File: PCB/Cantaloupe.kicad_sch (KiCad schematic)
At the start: 117 parts, among them J1 RGB_Out, J2 SWD, J3 Trackpad, J4 OLED, J5 Extra, J6 USB_In, J7 Split_comm_link, Q1 AO6802, SW1 MX, SW10 MX, SW11 MX, SW12 MX, SW13 MX, SW14 MX, SW15 MX, SW16 MX, SW17 MX, SW18 MX, SW19 MX, SW2 MX, SW20 MX, SW21 MX, SW22 MX, SW23 MX, SW24 MX, SW25 MX, SW26 MX, SW27 MX, SW28 MX, SW29 MX, SW3 MX, SW30 MX, SW31 Encoder, SW32 Reset, SW4 MX, SW5 MX, SW6 MX, SW7 MX, SW8 MX, SW9 MX, U1 STM32F401CCU6, U2 MB85RS64, U3 SRV05-4, U4 SRV05-4, U5 W25Q128JVS, U6 XC6206P332MR, Y1 8MHz

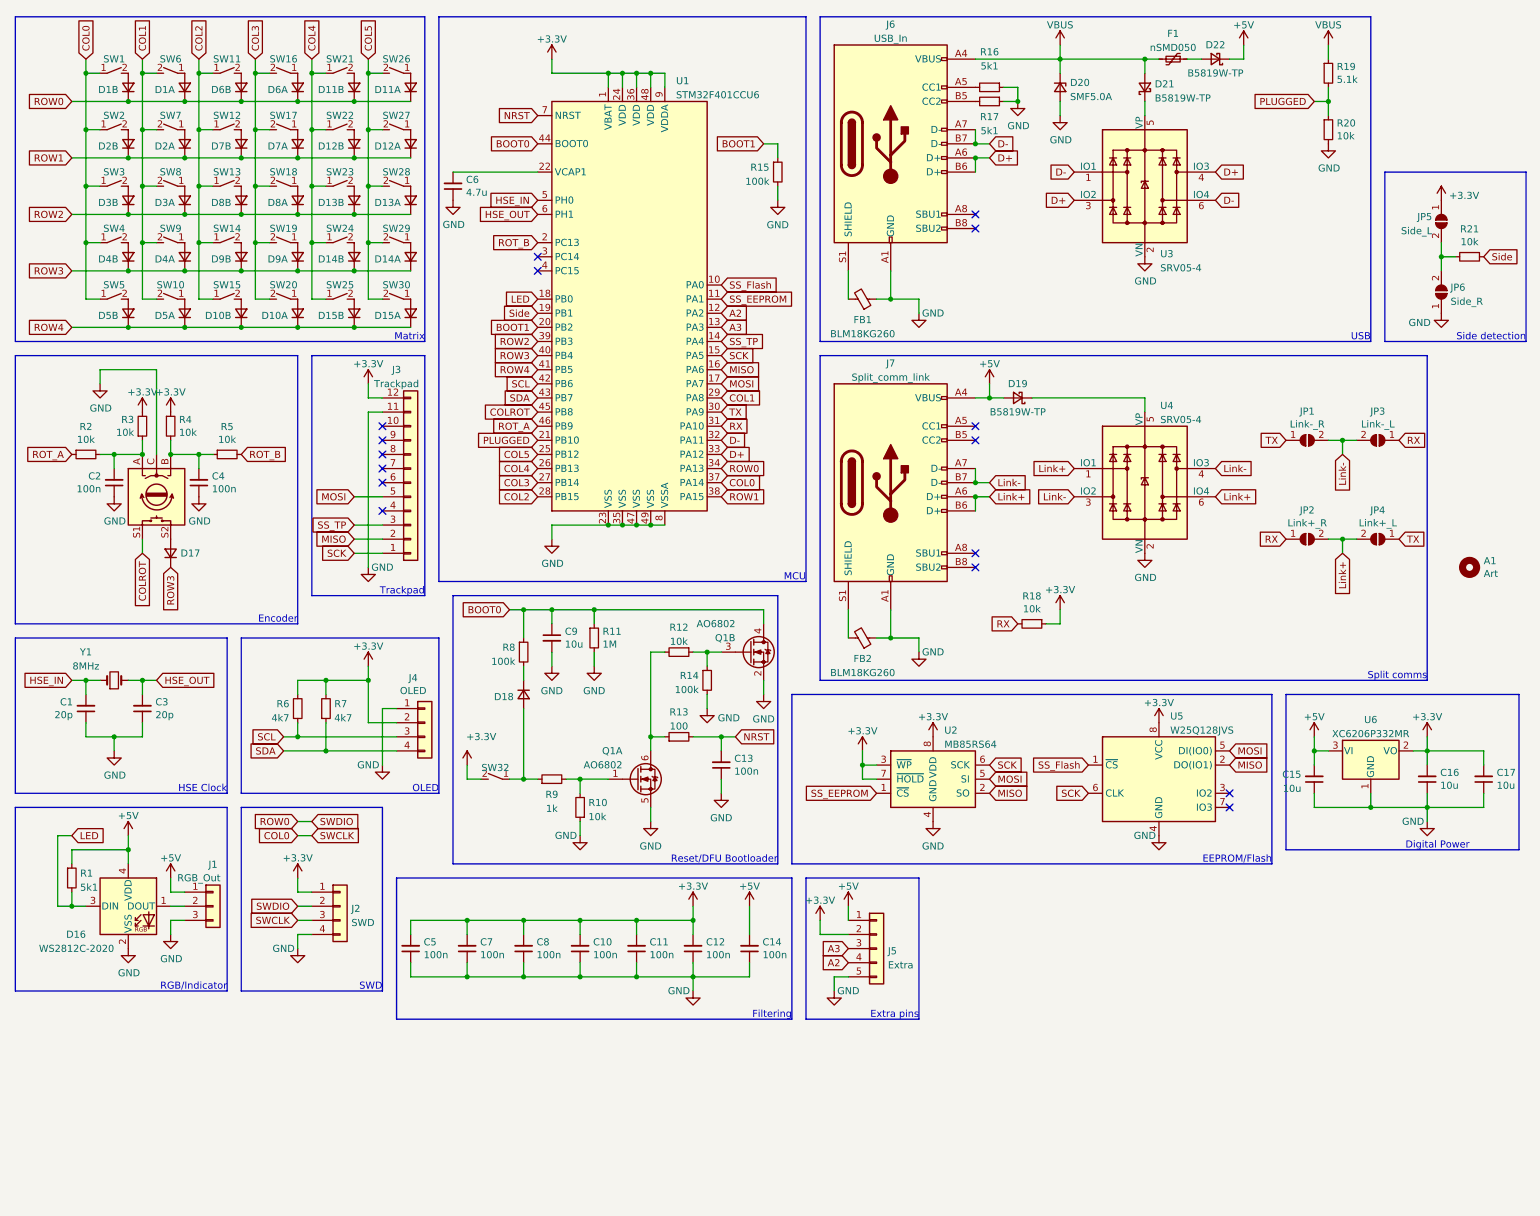
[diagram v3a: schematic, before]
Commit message: 30/5/2022 changes
Changed XC6206P332MR-G to XC6220B331MR-G for more power output. Changed fuse to 1A. Fixed library links. Changed AO6802 back to two AO3400s. Moved reset circuit downwards and extra pin header upwards for better routing. Updated BOM.
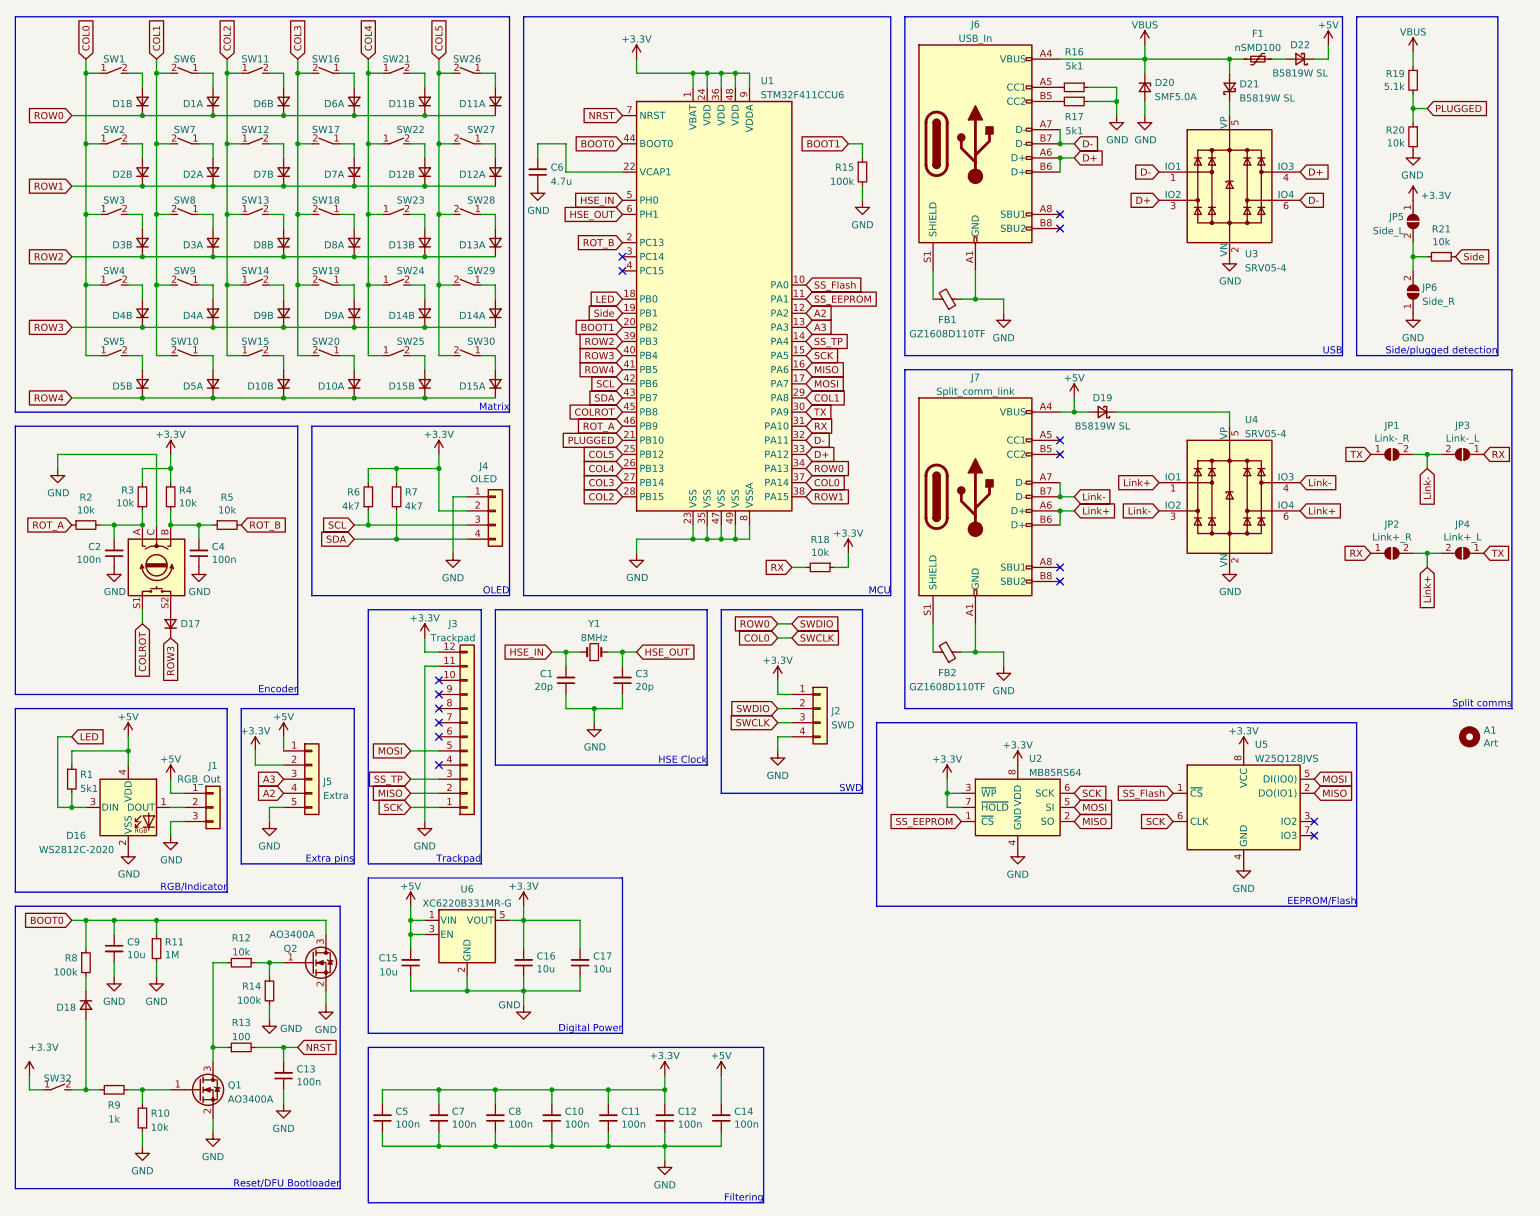
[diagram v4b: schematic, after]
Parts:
- removed Q1: AO6802, Package_TO_SOT_SMD:SOT-23-6, symbol Device:Q_Dual_NMOS_G1S2G2D2S1D1
- removed U6: XC6206P332MR, Package_TO_SOT_SMD:SOT-23, symbol Regulator_Linear:XC6206PxxxMR
- added Q1, Q2: AO3400A, Package_TO_SOT_SMD:SOT-23, symbol Transistor_FET:AO3400A
- added U6: XC6220B331MR-G, Package_TO_SOT_SMD:SOT-23-5, symbol Regulator_Linear:AP2112K-3.3
- A1: footprint Ariamelon:Ariamelon_Logo_x3_CU -> Cantaloupe:Ariamelon_Logo_x3_CU
- D1, D10, D11, D12, D13, D14, D15, D2, D3, D4, D5, D6, D7, D8, D9: symbol Ariamelon:D_Dual_CommonCathode_AAK_Split_Small -> Cantaloupe:D_Dual_CommonCathode_AAK_Split_Small
- D16: footprint Ariamelon:LED_WS2812-2020_Flippable -> Cantaloupe:LED_WS2812-2020_Flippable; LCSC part number C965556 -> C2976072
- D17, D18, D20: footprint Ariamelon:D_SOD-123 -> Cantaloupe:D_SOD-123
- D19, D21, D22: value B5819W-TP -> B5819W SL; footprint Ariamelon:D_SOD-123 -> Cantaloupe:D_SOD-123
- F1: value nSMD050 -> nSMD100; LCSC part number C69688 -> C66453
- FB1, FB2: value BLM18KG260 -> GZ1608D110TF; LCSC part number C88981 -> C74329
- J1: footprint Ariamelon:PinHeader_1x03_P2.54mm_Vertical_Silkless -> Cantaloupe:PinHeader_1x03_P2.54mm_Vertical_Silkless
- J2: footprint Ariamelon:PinHeader_1x04_P2.54mm_Vertical_SIlkless -> Cantaloupe:PinHeader_1x04_P2.54mm_Vertical_SIlkless
- J3: footprint Ariamelon:Hirose_FH12-12S-0.5SH_1x12-1MP_P0.50mm_Horizontal_Flippable -> Cantaloupe:Hirose_FH12-12S-0.5SH_1x12-1MP_P0.50mm_Horizontal_Flippable
- J4: footprint Ariamelon:OLED_0.96_SSD1306_128x64_Flippable_Reversepads -> Cantaloupe:OLED_0.96_SSD1306_128x64_Flippable_Reversepads
- J5: footprint Ariamelon:PinHeader_1x05_P2.54mm_Vertical_Silkless -> Cantaloupe:PinHeader_1x05_P2.54mm_Vertical_Silkless
- J6, J7: footprint Ariamelon:HRO-TYPE-C-31-M-13x -> Cantaloupe:HRO-TYPE-C-31-M-13x; symbol Ariamelon:USB_C_Receptacle_USB2.0-Connector -> Cantaloupe:USB_C_Receptacle_USB2.0-Connector
- SW1, SW10, SW11, SW12, SW13, SW14, SW15, SW16, SW17, SW18, SW19, SW2, SW20, SW21, SW22, SW23, SW24, SW25, SW26, SW27, SW28, SW29, SW3, SW30, SW4, SW5, SW6, SW7, SW8, SW9: footprint Ariamelon:MXOnly-1U-Hotswap-Dual -> Cantaloupe:MXOnly-1U-Hotswap-Dual; symbol Ariamelon:SW_SPST_Small -> Cantaloupe:SW_SPST_Small
- SW31: footprint Ariamelon:EC11_Flippable -> Cantaloupe:EC11_Flippable
- SW32: footprint Ariamelon:Switch_TS24ZJ_Flippable -> Cantaloupe:Switch_TS24ZJ_Flippable; symbol Ariamelon:SW_SPST_Small -> Cantaloupe:SW_SPST_Small
- U1: value STM32F401CCU6 -> STM32F411CCU6
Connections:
- net +3V3: now also SW32.1 (A), U6.5 (VOUT); no longer SW32.2 (B)
- net +5V: now also U6.1 (VIN), U6.3 (EN)
- net BOOT0: now also Q2.3 (D)
- net GND: now also Q1.2 (S), Q2.2 (S), U6.2 (GND)
- net at D18.2 (A), R9.1: now also SW32.2 (B); no longer SW32.1 (A)
- net at R10.2, R9.2: now also Q1.1 (G)
- net at R12.2, R13.1: now also Q1.3 (D)
- net at R12.1, R14.1: now also Q2.1 (G)
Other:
- note added: "Side/plugged detection"
- note removed: "Side detection"
- title: (none) -> Cantaloupe split ergonomic keyboard
- moved on the sheet: A1, C1, C10, C11, C12, C13, C14, C15, C17, C2, C3, C4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

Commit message: Better routing
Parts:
- SW1, SW10, SW11, SW12, SW13, SW14, SW15, SW16, SW17, SW18, SW19, SW2, SW20, SW21, SW22, SW23, SW24, SW25, SW26, SW27, SW28, SW29, SW3, SW30, SW4, SW5, SW6, SW7, SW8, SW9: footprint Cantaloupe:MXOnly-1U-Hotswap-Dual -> Cantaloupe:MX_Choc-1U-Hotswap-Dual

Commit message: INCOMPLETE V3.0 Initial Update
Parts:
- removed C1, C3: 20p, Capacitor_SMD:C_0603_1608Metric, symbol Device:C_Small
- removed C10, C11, C12, C13, C14, C2, C4, C5, C7, C8: 100n, Capacitor_SMD:C_0603_1608Metric, symbol Device:C_Small
- removed C15, C16, C17, C9: 10u, Capacitor_SMD:C_0603_1608Metric, symbol Device:C_Small
- removed C6: 4.7u, Capacitor_SMD:C_0603_1608Metric, symbol Device:C_Small
- removed D1, D10, D11, D12, D13, D14, D15, D2, D3, D4, D5, D6, D7, D8, D9: D_Dual_CommonCathode_AAK_Split_Small, Package_TO_SOT_SMD:SOT-23, symbol Cantaloupe:D_Dual_CommonCathode_AAK_Split_Small
- removed D16: WS2812C-2020, Cantaloupe:LED_WS2812-2020_Flippable, symbol LED:SK6812MINI
- removed D17, D18: D, Cantaloupe:D_SOD-123, symbol Device:D_Small
- removed D19, D21, D22: B5819W SL, Cantaloupe:D_SOD-123, symbol Device:D_Schottky_Small
- removed D20: SMF5.0A, Cantaloupe:D_SOD-123, symbol Device:D_Zener_Small
- removed F1: nSMD100, Fuse:Fuse_1206_3216Metric, symbol Device:Polyfuse_Small
- removed FB1, FB2: GZ1608D110TF, Inductor_SMD:L_0603_1608Metric, symbol Djinn-rescue:Ferrite_Bead_Small-Device
- removed J1: RGB_Out, Cantaloupe:PinHeader_1x03_P2.54mm_Vertical_Silkless, symbol Connector_Generic:Conn_01x03
- removed J2: SWD, Cantaloupe:PinHeader_1x04_P2.54mm_Vertical_SIlkless, symbol Connector_Generic:Conn_01x04
- removed J3: Trackpad, Cantaloupe:Hirose_FH12-12S-0.5SH_1x12-1MP_P0.50mm_Horizontal_Flippable, symbol Connector_Generic:Conn_01x12
- removed J4: OLED, Cantaloupe:OLED_0.96_SSD1306_128x64_Flippable_Reversepads, symbol Connector_Generic:Conn_01x04
- removed J5: Extra, Cantaloupe:PinHeader_1x05_P2.54mm_Vertical_Silkless, symbol Connector_Generic:Conn_01x05
- removed J6: USB_In, Cantaloupe:HRO-TYPE-C-31-M-13x, symbol Cantaloupe:USB_C_Receptacle_USB2.0-Connector
- removed J7: Split_comm_link, Cantaloupe:HRO-TYPE-C-31-M-13x, symbol Cantaloupe:USB_C_Receptacle_USB2.0-Connector
- removed JP1: Link-_R, Jumper:SolderJumper-2_P1.3mm_Open_Pad1.0x1.5mm, symbol Jumper:SolderJumper_2_Open
- removed JP2: Link+_R, Jumper:SolderJumper-2_P1.3mm_Open_Pad1.0x1.5mm, symbol Jumper:SolderJumper_2_Open
- removed JP3: Link-_L, Jumper:SolderJumper-2_P1.3mm_Open_Pad1.0x1.5mm, symbol Jumper:SolderJumper_2_Open
- removed JP4: Link+_L, Jumper:SolderJumper-2_P1.3mm_Open_Pad1.0x1.5mm, symbol Jumper:SolderJumper_2_Open
- removed JP5: Side_L, Jumper:SolderJumper-2_P1.3mm_Open_Pad1.0x1.5mm, symbol Jumper:SolderJumper_2_Open
- removed JP6: Side_R, Jumper:SolderJumper-2_P1.3mm_Open_Pad1.0x1.5mm, symbol Jumper:SolderJumper_2_Open
- removed Q1, Q2: AO3400A, Package_TO_SOT_SMD:SOT-23, symbol Transistor_FET:AO3400A
- removed R1, R16, R17: 5k1, Resistor_SMD:R_0603_1608Metric, symbol Device:R_Small
- removed R10, R12, R18, R2, R20, R21, R3, R4, R5: 10k, Resistor_SMD:R_0603_1608Metric, symbol Device:R_Small
- removed R11: 1M, Resistor_SMD:R_0603_1608Metric, symbol Device:R_Small
- removed R13: 100, Resistor_SMD:R_0603_1608Metric, symbol Device:R_Small
- removed R14, R15, R8: 100k, Resistor_SMD:R_0603_1608Metric, symbol Device:R_Small
- removed R19: 5.1k, Resistor_SMD:R_0603_1608Metric, symbol Device:R_Small
- removed R6, R7: 4k7, Resistor_SMD:R_0603_1608Metric, symbol Device:R_Small
- removed R9: 1k, Resistor_SMD:R_0603_1608Metric, symbol Device:R_Small
- removed SW1, SW10, SW11, SW12, SW13, SW14, SW15, SW16, SW17, SW18, SW19, SW2, SW20, SW21, SW22, SW23, SW24, SW25, SW26, SW27, SW28, SW29, SW3, SW30, SW4, SW5, SW6, SW7, SW8, SW9: MX, Cantaloupe:MX_Choc-1U-Hotswap-Dual, symbol Cantaloupe:SW_SPST_Small
- removed SW31: Encoder, Cantaloupe:EC11_Flippable, symbol Device:Rotary_Encoder_Switch
- removed SW32: Reset, Cantaloupe:Switch_TS24ZJ_Flippable, symbol Cantaloupe:SW_SPST_Small
- removed U1: STM32F411CCU6, Package_DFN_QFN:QFN-48-1EP_7x7mm_P0.5mm_EP5.6x5.6mm, symbol MCU_ST_STM32F4:STM32F411CCUx
- removed U2: MB85RS64, Package_SO:SSOP-8_3.9x5.05mm_P1.27mm, symbol Memory_NVRAM:MB85RS64
- removed U3, U4: SRV05-4, Package_TO_SOT_SMD:SOT-23-6, symbol Power_Protection:SRV05-4
- removed U5: W25Q128JVS, Package_SO:SOIC-8_5.275x5.275mm_P1.27mm, symbol Memory_Flash:W25Q128JVS
- removed U6: XC6220B331MR-G, Package_TO_SOT_SMD:SOT-23-5, symbol Regulator_Linear:AP2112K-3.3
- removed Y1: 8MHz, Crystal:Crystal_SMD_5032-2Pin_5.0x3.2mm, symbol Device:Crystal_Small
- added H1, H2, H3: Tooling Hole, Cantaloupe:JLC Tooling Hole, symbol Mechanical:MountingHole
- A1: symbol Mechanical:MountingHole -> Mechanical:Fiducial; now in the parts list
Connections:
- no-connect marks 16 -> 0
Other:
- added sheet Comms (Comms.kicad_sch)
- added sheet MCU (MCU.kicad_sch)
- added sheet Matrix (Matrix.kicad_sch)
- added sheet PSU (PSU.kicad_sch)
- added sheet RGB (RGB.kicad_sch)
- note removed: "Digital Power"
- note removed: "EEPROM/Flash"
- note removed: "Encoder"
- note removed: "Extra pins"
- note removed: "Filtering"
- note removed: "HSE Clock"
- note removed: "MCU"
- note removed: "Matrix"
- note removed: "OLED"
- note removed: "RGB/Indicator"
- note removed: "Reset/DFU Bootloader"
- note removed: "SWD"
- note removed: "Side/plugged detection"
- note removed: "Split comms"
- note removed: "Trackpad"
- note removed: "USB"

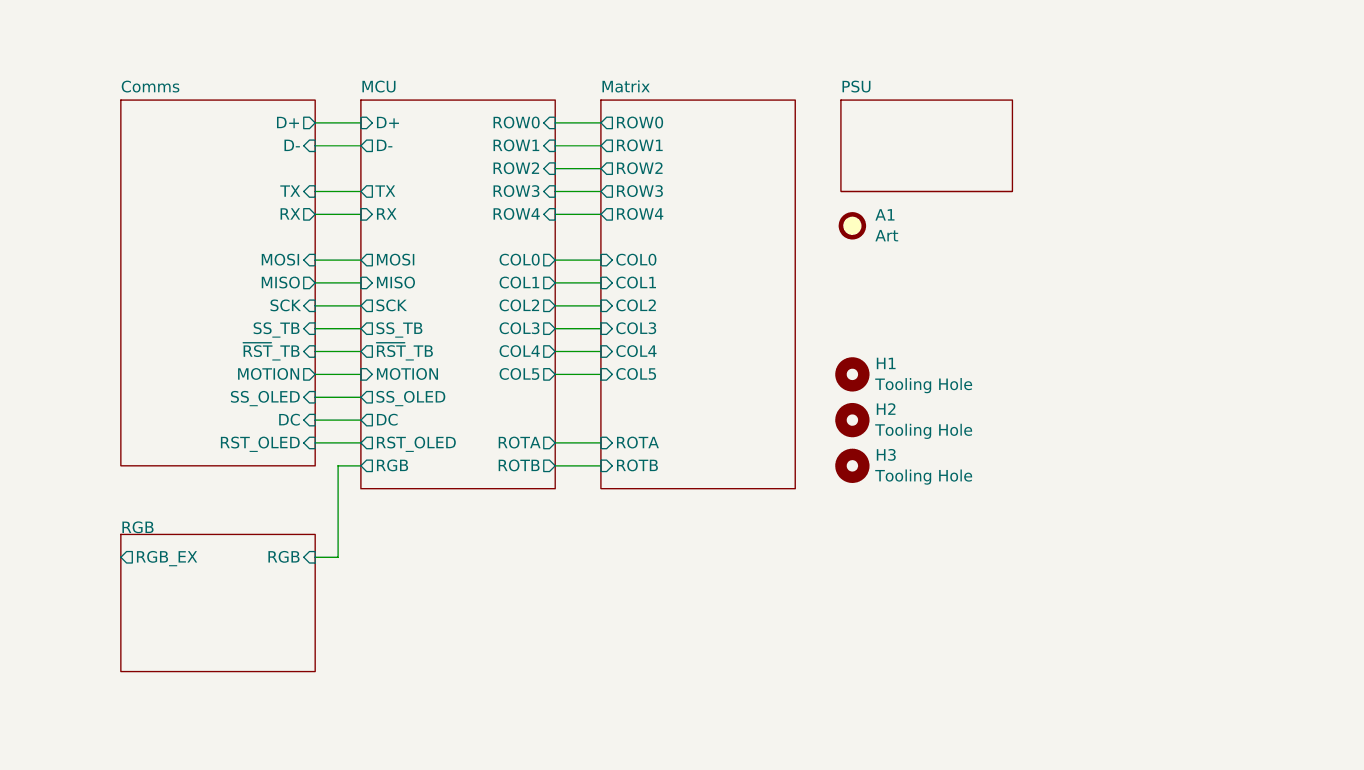
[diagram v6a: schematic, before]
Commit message: 08/08/2023 update
Removed Ogen footprint, and future VIK support is planned. Rerouted board following latest Honeydew revision. WIP support for the USB2541 is added, but it's very tentative and not yet complete. Added CX70M-24P1 footprint.
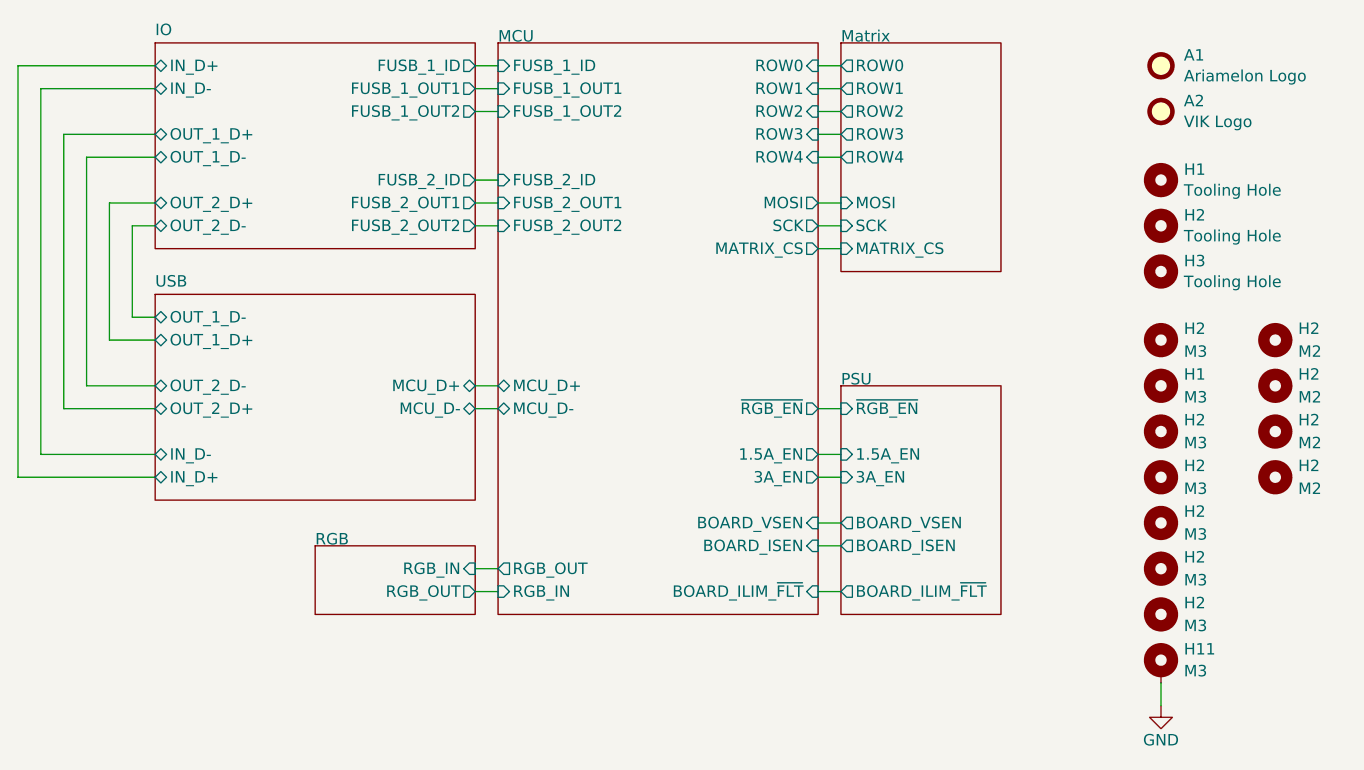
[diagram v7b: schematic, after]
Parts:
- removed H1, H2: Tooling Hole, Cantaloupe:JLC Tooling Hole, symbol Mechanical:MountingHole
- added A2: VIK Logo, Cantaloupe:vik-logo-medium, symbol Mechanical:Fiducial
- added H1, H2 (x6): M3, Cantaloupe:MountingHole_3.2mm_M3_Pad, symbol Mechanical:MountingHole
- added H1, H2: Tooling Hole, Cantaloupe:JLC Tooling Hole, symbol Mechanical:MountingHole
- added H11: M3, Cantaloupe:MountingHole_3.2mm_M3_Pad, symbol Honeydew:MountingHole_Pad
- added H2 (x4): M2, MountingHole:MountingHole_2.2mm_M2_Pad, symbol Mechanical:MountingHole
- A1: value Art -> Ariamelon Logo; footprint Cantaloupe:Ariamelon_Logo_x3_CU -> Cantaloupe:Ariamelon_Logo_x3_Mask; now left out of the parts list
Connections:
- new net GND: H11.1
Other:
- removed sheet Comms
- added sheet IO (IO.kicad_sch)
- added sheet USB (USB.kicad_sch)
- sheet MCU ports: added 1.5A_EN, 3A_EN, BOARD_ILIM_~{FLT}, BOARD_ISEN, BOARD_VSEN, FUSB_1_ID, FUSB_1_OUT1, FUSB_1_OUT2, FUSB_2_ID, FUSB_2_OUT1, FUSB_2_OUT2, MATRIX_CS, MCU_D+, MCU_D-, RGB_IN, RGB_OUT, ~{RGB_EN}; removed COL0, COL1, COL2, COL3, COL4, COL5, D+, D-, DC, MISO, MOTION, RGB, ROTA, ROTB, RST_OLED, RX, SS_OLED, SS_TB, TX, ~{RST}_TB
- sheet Matrix ports: added MATRIX_CS, MOSI, SCK; removed COL0, COL1, COL2, COL3, COL4, COL5, ROTA, ROTB
- sheet PSU ports: added 1.5A_EN, 3A_EN, BOARD_ILIM_~{FLT}, BOARD_ISEN, BOARD_VSEN, ~{RGB_EN}; removed none
- sheet RGB ports: added RGB_IN, RGB_OUT; removed RGB, RGB_EX
- company: (none) -> Created by Ariamelon (https://github.com/Ariamelon/Cantaloupe/)
- moved on the sheet: A1
